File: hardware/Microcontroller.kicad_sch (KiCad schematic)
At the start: 34 parts, among them J1 USB_B_Micro, J2 SM03B-SRSS-TB, SW1 SW_Push, SW2 SW_Push, U1 W25Q128JVS, U2 NCP1117-3.3_SOT223, U3 RP2350_60QFN, Y1 ABM8-272-T3

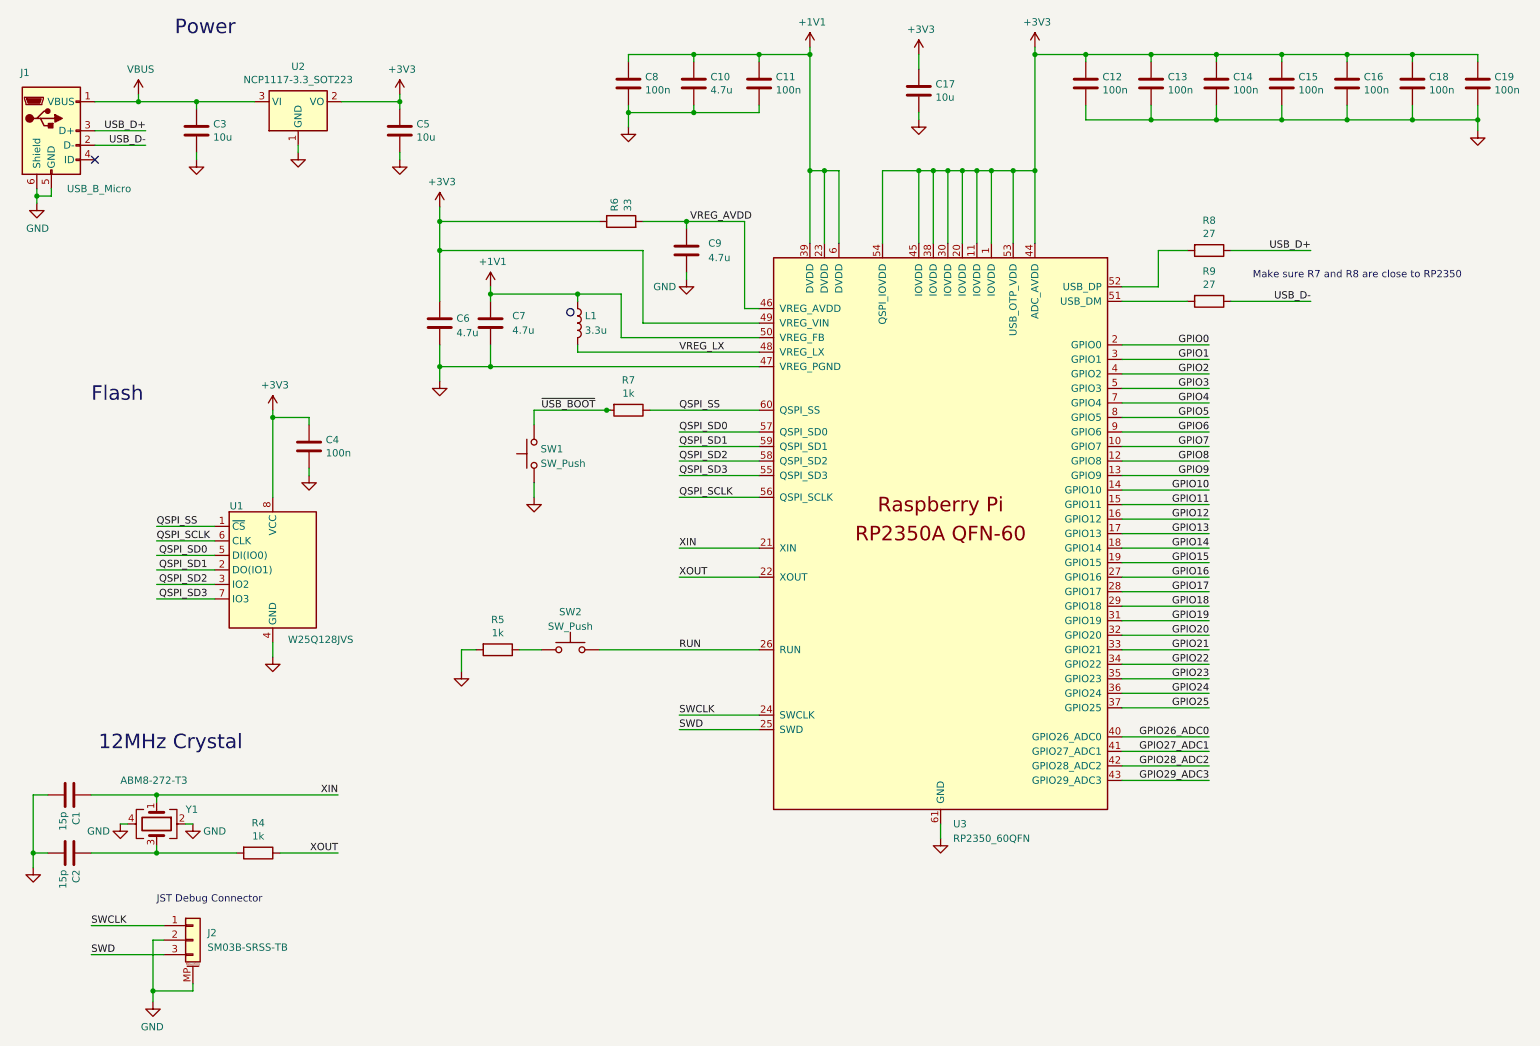
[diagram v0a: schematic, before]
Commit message: WIP checkin * Added most of the JLCPCB part numbers * Added most of the component footprints * Connected up microcontroller and dc/dc converter
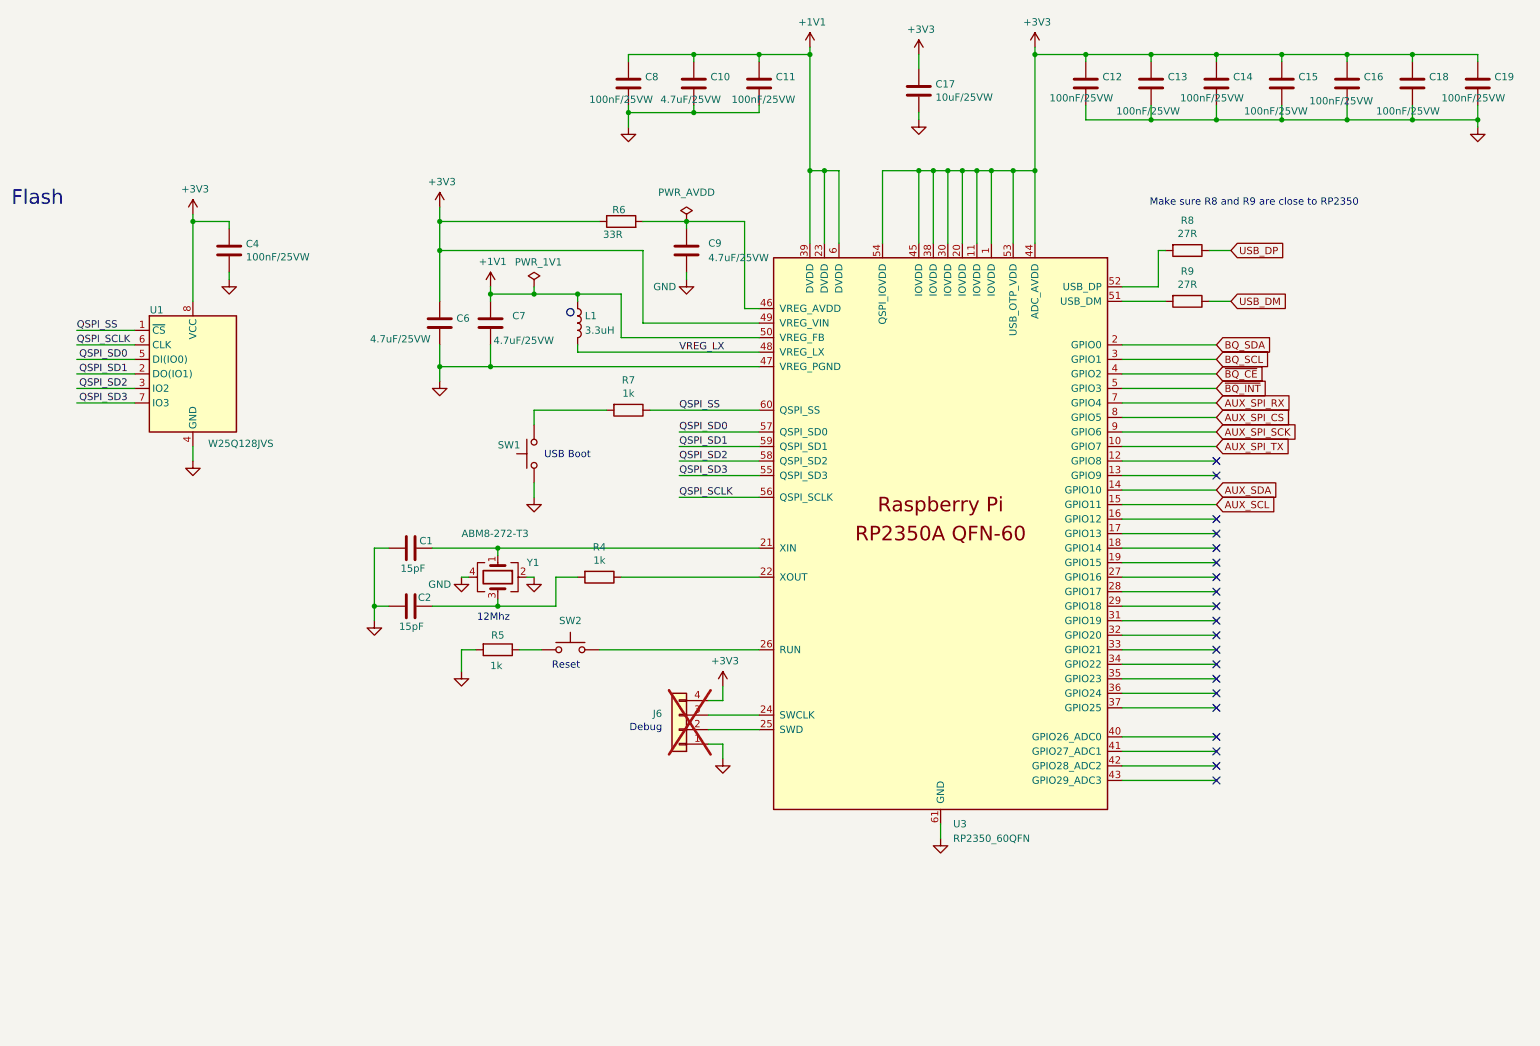
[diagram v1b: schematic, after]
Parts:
- removed C3, C5: 10u, Capacitor_SMD:C_0805_2012Metric, symbol Device:C
- removed J1: USB_B_Micro, Connector_USB:USB_Micro-B_Amphenol_10103594-0001LF_Horizontal, symbol Connector:USB_B_Micro
- removed J2: SM03B-SRSS-TB, Connector_JST:JST_SH_SM03B-SRSS-TB_1x03-1MP_P1.00mm_Horizontal, symbol Connector_Generic_MountingPin:Conn_01x03_MountingPin
- removed U2: NCP1117-3.3_SOT223, Package_TO_SOT_SMD:SOT-223-3_TabPin2, symbol Regulator_Linear:NCP1117-3.3_SOT223
- added J6: CON4, Connector_PinHeader_2.54mm:PinHeader_1x04_P2.54mm_Vertical, symbol Connector_Generic:Conn_01x04
- C1, C2: value 15p -> 15pF; JLCPCB (none) -> C1548
- C10, C9: value 4.7u -> 4.7uF/25VW; footprint Capacitor_SMD:C_0402_1005Metric -> Capacitor_SMD:C_0805_2012Metric; JLCPCB (none) -> C1779
- C11, C12, C13, C14, C15, C16, C18, C19, C4, C8: value 100n -> 100nF/25VW; footprint Capacitor_SMD:C_0402_1005Metric -> Capacitor_SMD:C_0603_1608Metric; JLCPCB (none) -> C1590
- C17: value 10u -> 10uF/25VW; JLCPCB (none) -> C15850
- C6, C7: value 4.7u -> 4.7uF/25VW; footprint RP2350_60QFN_minimal:C_0402_1005Metric_small_pads -> Capacitor_SMD:C_0805_2012Metric; JLCPCB (none) -> C1779
- L1: value 3.3u -> 3.3uH; JLCPCB (none) -> C42411119
- R4, R5, R7: footprint Resistor_SMD:R_0402_1005Metric -> Resistor_SMD:R_0603_1608Metric; JLCPCB (none) -> C21190
- R6: value 33 -> 33R; footprint Resistor_SMD:R_0402_1005Metric -> Resistor_SMD:R_0603_1608Metric; JLCPCB (none) -> C23140
- R8, R9: value 27 -> 27R; footprint Resistor_SMD:R_0402_1005Metric -> Resistor_SMD:R_0603_1608Metric; JLCPCB (none) -> C25190
- SW1, SW2: footprint Button_Switch_SMD:SW_Push_1P1T_NO_Vertical_Wuerth_434133025816 -> BidirectionalSupply:TS-1088-AR02016; JLCPCB (none) -> C720477
- U1: JLCPCB (none) -> C97521
- U3: JLCPCB (none) -> C42411118
- Y1: JLCPCB (none) -> C20625731
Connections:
- net +3V3: now also J6.4 (Pin_4)
- net GND: now also J6.1 (Pin_1)
- net GPIO0 renamed BQ_SDA
- net GPIO1 renamed BQ_SCL
- net GPIO10 renamed AUX_SDA
- net GPIO11 renamed AUX_SCL
- net GPIO12: no longer names the net of U3.16 (GPIO12)
- net GPIO13: no longer names the net of U3.17 (GPIO13)
- net GPIO14: no longer names the net of U3.18 (GPIO14)
- net GPIO15: no longer names the net of U3.19 (GPIO15)
- net GPIO16: no longer names the net of U3.27 (GPIO16)
- net GPIO17: no longer names the net of U3.28 (GPIO17)
- net GPIO18: no longer names the net of U3.29 (GPIO18)
- net GPIO19: no longer names the net of U3.31 (GPIO19)
- net GPIO2 renamed ~{BQ_CE}
- net GPIO20: no longer names the net of U3.32 (GPIO20)
- net GPIO21: no longer names the net of U3.33 (GPIO21)
- net GPIO22: no longer names the net of U3.34 (GPIO22)
- net GPIO23: no longer names the net of U3.35 (GPIO23)
- net GPIO24: no longer names the net of U3.36 (GPIO24)
- net GPIO25: no longer names the net of U3.37 (GPIO25)
- net GPIO26_ADC0: no longer names the net of U3.40 (GPIO26_ADC0)
- net GPIO27_ADC1: no longer names the net of U3.41 (GPIO27_ADC1)
- net GPIO28_ADC2: no longer names the net of U3.42 (GPIO28_ADC2)
- net GPIO29_ADC3: no longer names the net of U3.43 (GPIO29_ADC3)
- net GPIO3 renamed ~{BQ_INT}
- net GPIO4 renamed AUX_SPI_RX
- net GPIO5 renamed AUX_SPI_CS
- net GPIO6 renamed AUX_SPI_SCK
- net GPIO7 renamed AUX_SPI_TX
- net GPIO8: no longer names the net of U3.12 (GPIO8)
- net GPIO9: no longer names the net of U3.13 (GPIO9)
- net RUN: no longer names the net of SW2.2, U3.26 (RUN)
- net SWCLK: no longer names the net of U3.24 (SWCLK)
- net SWCLK: now also J6.3 (Pin_3)
- net SWD: no longer names the net of U3.25 (SWD)
- net SWD: now also J6.2 (Pin_2)
- net USB_D+ renamed USB_DP
- net USB_D- renamed USB_DM
- net VREG_AVDD: no longer names the net of C9.1, R6.2, U3.46 (VREG_AVDD)
- net XIN: no longer names the net of C1.1, U3.21 (XIN), Y1.1
- net XOUT: no longer names the net of R4.1, U3.22 (XOUT)
- net ~{USB_BOOT}: no longer names the net of R7.2, SW1.2
- no-connect marks 1 -> 20
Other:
- note added: "12Mhz"
- note added: "Debug"
- note added: "Make sure R8 and R9 are close to RP2350"
- note added: "Reset"
- note added: "USB Boot"
- note removed: "12MHz Crystal"
- note removed: "JST Debug Connector"
- note removed: "Make sure R7 and R8 are close to RP2350"
- note removed: "Power"
- company: (none) -> Open Source Solutions Pty Ltd
- title: (none) -> Microcontroller
- moved on the sheet: C1, C2, C4, R4, R8, R9, U1, Y1

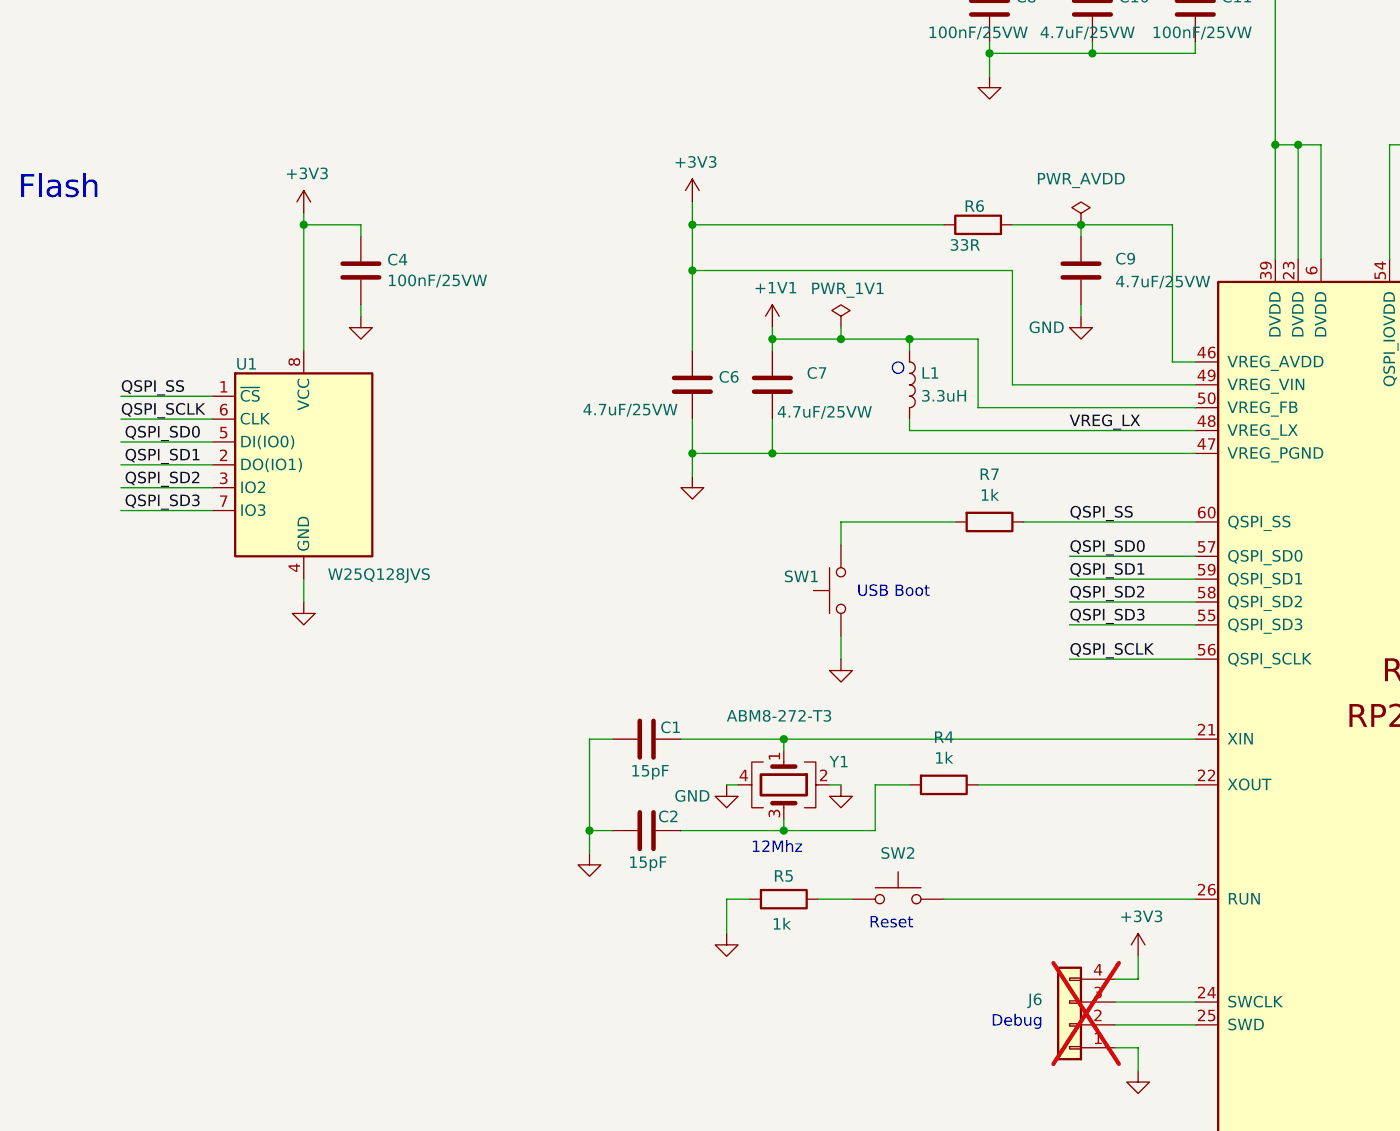
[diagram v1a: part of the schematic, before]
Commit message: Cleaned up share library Added switchmode 3v3 supply
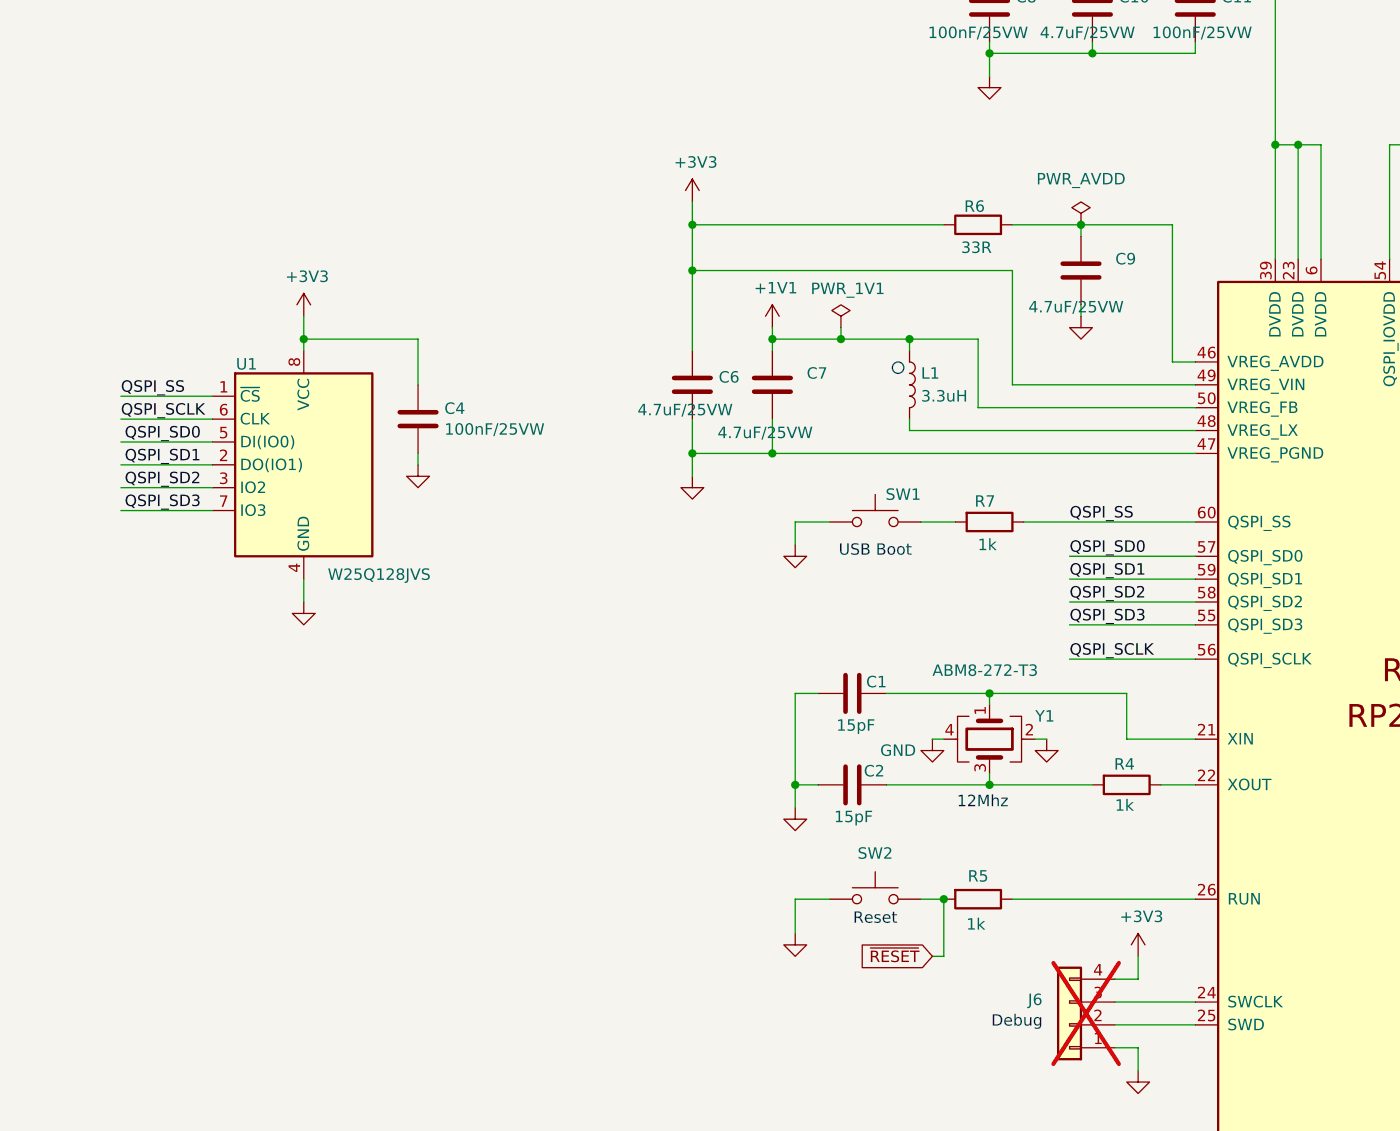
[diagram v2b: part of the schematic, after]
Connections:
- net GND: now also SW2.1; no longer R5.2
- net at R5.1: now also U3.26 (RUN); no longer SW2.1
- net ~{RESET}: now reaches SW2.2
- net ~{RESET}: now also R5.2; no longer U3.26 (RUN)
- net VREG_LX: no longer names the net of L1.2, U3.48 (VREG_LX)
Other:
- note removed: "Flash"
- moved on the sheet: C1, C2, C4, R4, R5, SW1, SW2, Y1

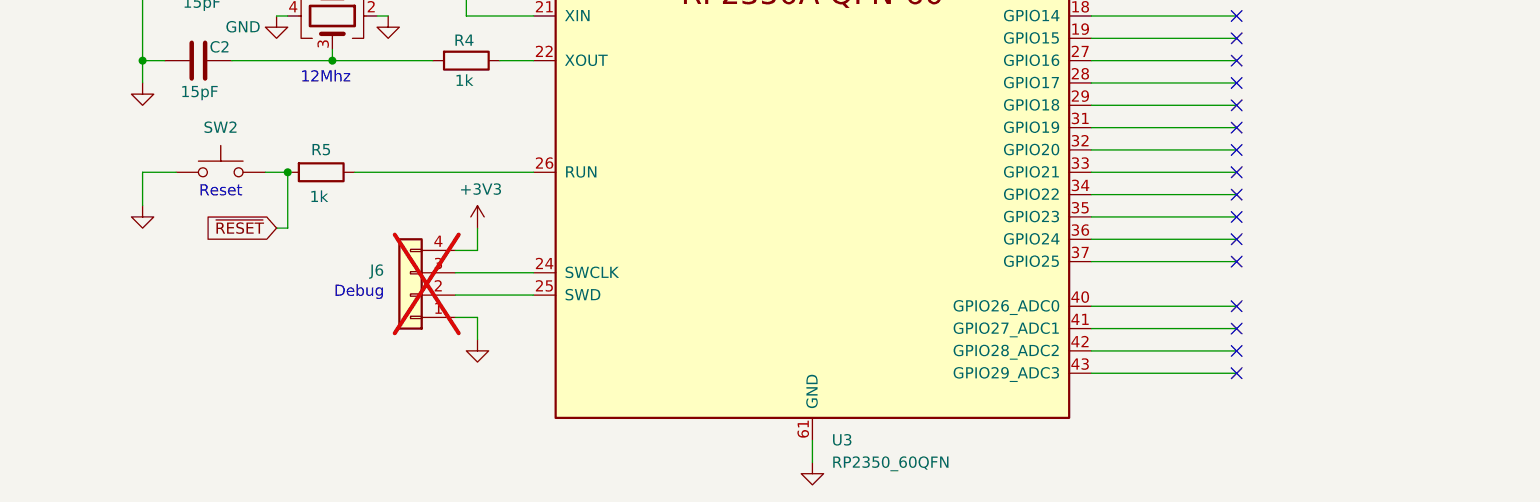
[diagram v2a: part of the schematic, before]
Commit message: Schematic is now mostly complete. Will review and then move onto the PCB layout
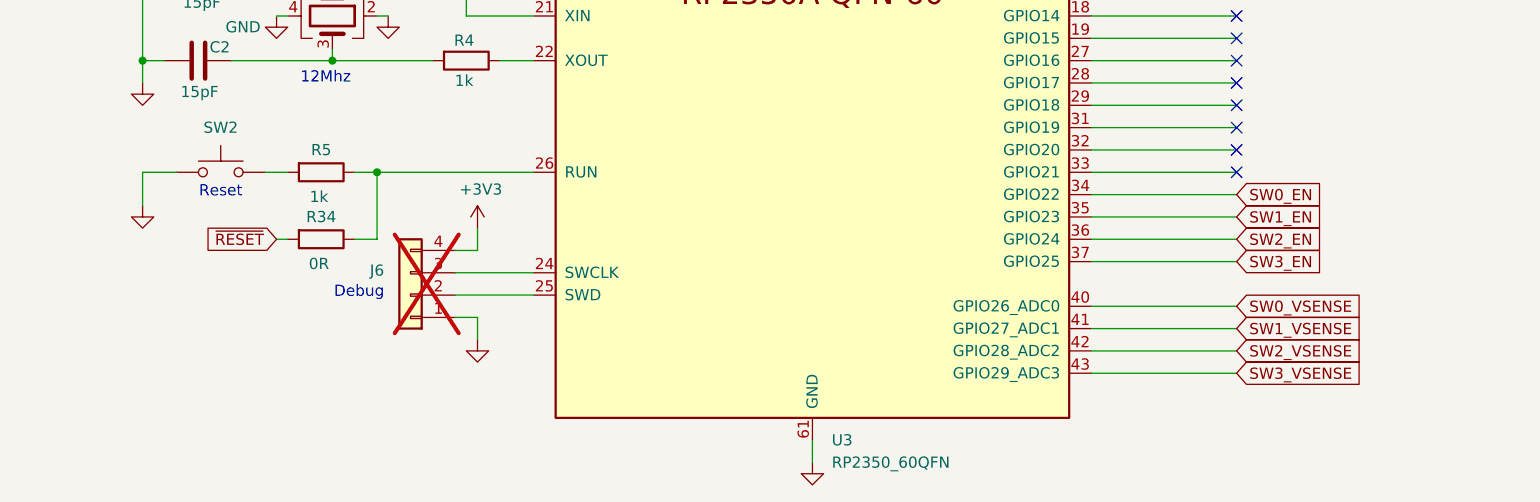
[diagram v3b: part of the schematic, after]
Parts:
- added R34: 0R, Resistor_SMD:R_0603_1608Metric, symbol Device:R
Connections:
- net ~{RESET}: now also R34.2; no longer R5.2, SW2.2
- net at R5.1, U3.26 (RUN): now also R34.1
- net SW0_EN: now reaches U3.34 (GPIO22)
- net SW1_EN: now reaches U3.35 (GPIO23)
- net SW2_EN: now reaches U3.36 (GPIO24)
- net SW3_EN: now reaches U3.37 (GPIO25)
- net SW0_VSENSE: now reaches U3.40 (GPIO26_ADC0)
- net SW1_VSENSE: now reaches U3.41 (GPIO27_ADC1)
- net SW2_VSENSE: now reaches U3.42 (GPIO28_ADC2)
- net SW3_VSENSE: now reaches U3.43 (GPIO29_ADC3)
- new net: R5.2, SW2.2
- no-connect marks 20 -> 12

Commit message: Checked all DC/DC converter capacitors Some part substitution to preference in stock items
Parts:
- added D15: RED, LED_SMD:LED_0603_1608Metric, symbol Device:LED
- added J11: Conn_01x08, Connector_PinHeader_2.54mm:PinHeader_1x08_P2.54mm_Vertical, symbol Connector_Generic:Conn_01x08
- added R58: 1k, Resistor_SMD:R_0603_1608Metric, symbol Device:R
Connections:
- net +3V3: now also R58.1
- net LED: now reaches U3.12 (GPIO8)
- net LED: now also D15.1 (K)
- net at U3.16 (GPIO12): now also J11.1 (Pin_1)
- net at U3.17 (GPIO13): now also J11.2 (Pin_2)
- net at U3.18 (GPIO14): now also J11.3 (Pin_3)
- net at U3.19 (GPIO15): now also J11.4 (Pin_4)
- net at U3.27 (GPIO16): now also J11.5 (Pin_5)
- net at U3.28 (GPIO17): now also J11.6 (Pin_6)
- net at U3.29 (GPIO18): now also J11.7 (Pin_7)
- net at U3.31 (GPIO19): now also J11.8 (Pin_8)
- new net: D15.2 (A), R58.2
- no-connect marks 12 -> 3
